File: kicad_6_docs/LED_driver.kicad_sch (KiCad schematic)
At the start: 18 parts, among them Q2 BC560, U14 SSI2164, U16 TL072

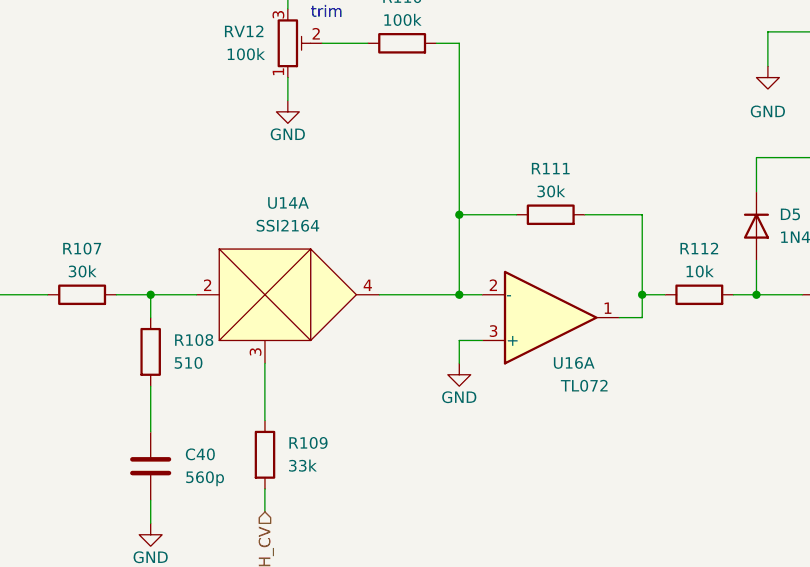
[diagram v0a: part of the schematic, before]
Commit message: Fix power supply errors, tidy up schematic
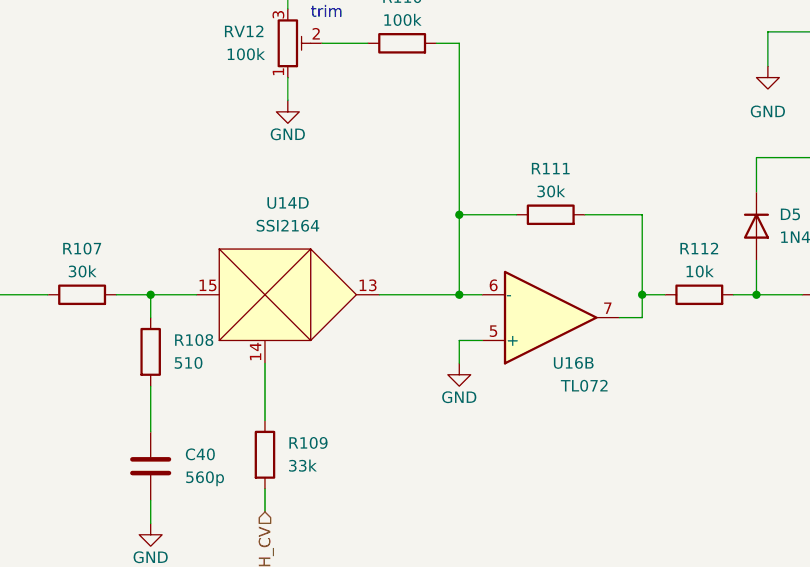
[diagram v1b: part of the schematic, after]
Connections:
- net GND: now also U16.5 (+); no longer U16.3 (+)
- net at R107.2, R108.1: now also U14.15; no longer U14.2
- net at R109.1: now also U14.14; no longer U14.3
- net at R110.2, R111.1: now also U14.13, U16.6 (-); no longer U14.4, U16.2 (-)
- net at R111.2, R112.1: now also U16.7; no longer U16.1
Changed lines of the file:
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@@
   (title_block
     (title "Mu-Tron Bi-Phase near-clone")
-    (date "2022-01-14")
+    (date "2022-08-01")
     (rev "0")
     (comment 2 "creativecommons.org/licenses/by/4.0/")
@@
     (effects (font (size 1.27 1.27)) (justify right))
   )
-  (symbol (lib_id "Device:LED") (at 194.31 111.76 90)
+  (symbol (lib_id "Device:LED") (at 194.31 111.76 90) (unit 1)
     (in_bom yes) (on_board yes) (fields_autoplaced)
     (property "Reference" "D7" (id 0) (at 198.12 112.0774 90)
@@
     (pin "2")
   )
-  (symbol (lib_id "Device:C") (at 114.3 109.22 0)
+  (symbol (lib_id "Device:C") (at 114.3 109.22 0) (unit 1)
     (in_bom yes) (on_board yes) (fields_autoplaced)
     (property "Reference" "C40" (id 0) (at 118.11 107.9499 0)
@@
     (pin "2")
   )
-  (symbol (lib_id "power:GND") (at 148.59 97.79 0)
+  (symbol (lib_id "power:GND") (at 148.59 97.79 0) (unit 1)
     (in_bom yes) (on_board yes)
     (property "Reference" "#PWR078" (id 0) (at 148.59 104.14 0)
@@
     (pin "1")
   )
-  (symbol (lib_id "power:GND") (at 114.3 115.57 0)
+  (symbol (lib_id "power:GND") (at 114.3 115.57 0) (unit 1)
     (in_bom yes) (on_board yes)
     (property "Reference" "#PWR075" (id 0) (at 114.3 121.92 0)
@@
     (pin "1")
   )
-  (symbol (lib_id "Device:R") (at 114.3 96.52 0)
+  (symbol (lib_id "Device:R") (at 114.3 96.52 0) (unit 1)
     (in_bom yes) (on_board yes) (fields_autoplaced)
     (property "Reference" "R108" (id 0) (at 116.84 95.2499 0)
@@
     (pin "2")
   )
-  (symbol (lib_id "custom_symbols:SSI2164") (at 127 90.17 0)
+  (symbol (lib_id "custom_symbols:SSI2164") (at 127 90.17 0) (unit 4)
     (in_bom yes) (on_board yes) (fields_autoplaced)
     (property "Reference" "U14" (id 0) (at 129.54 80.01 0))
@@
       (effects (font (size 1.27 1.27)) hide)
     )
+    (pin "2")
+    (pin "3")
+    (pin "4")
+    (pin "5")
+    (pin "6")
+    (pin "7")
+    (pin "10")
+    (pin "11")
+    (pin "12")
     (pin "13")
     (pin "14")
     (pin "15")
-  )
-  (symbol (lib_id "power:GND") (at 87.63 96.52 0)
+    (pin "1")
+    (pin "16")
+    (pin "8")
+    (pin "9")
+  )
+  (symbol (lib_id "power:GND") (at 87.63 96.52 0) (unit 1)
     (in_bom yes) (on_board yes)
     (property "Reference" "#PWR074" (id 0) (at 87.63 102.87 0)
@@
     (pin "1")
   )
-  (symbol (lib_id "power:GND") (at 129.54 68.58 0)
+  (symbol (lib_id "power:GND") (at 129.54 68.58 0) (unit 1)
     (in_bom yes) (on_board yes)
     (property "Reference" "#PWR077" (id 0) (at 129.54 74.93 0)
@@
     (pin "1")
   )
-  (symbol (lib_id "Diode:1N4148") (at 181.61 82.55 270)
+  (symbol (lib_id "Diode:1N4148") (at 181.61 82.55 270) (unit 1)
     (in_bom yes) (on_board yes) (fields_autoplaced)
     (property "Reference" "D5" (id 0) (at 184.15 81.2799 90)
@@
     (pin "2")
   )
-  (symbol (lib_id "biPhase_2-rescue:BC560") (at 191.77 90.17 0) (mirror x)
+  (symbol (lib_id "biPhase_2-rescue:BC560") (at 191.77 90.17 0) (mirror x) (unit 1)
     (in_bom yes) (on_board yes) (fields_autoplaced)
     (property "Reference" "Q2" (id 0) (at 196.85 88.265 0)
@@
     (pin "3")
   )
-  (symbol (lib_id "Device:LED") (at 194.31 101.6 90)
+  (symbol (lib_id "Device:LED") (at 194.31 101.6 90) (unit 1)
     (in_bom yes) (on_board yes) (fields_autoplaced)
     (property "Reference" "D6" (id 0) (at 198.12 101.9174 90)
@@
     (pin "2")
   )
-  (symbol (lib_id "Device:R") (at 106.68 90.17 90)
+  (symbol (lib_id "Device:R") (at 106.68 90.17 90) (unit 1)
     (in_bom yes) (on_board yes)
     (property "Reference" "R107" (id 0) (at 106.68 85.09 90))
@@
     (pin "2")
   )
-  (symbol (lib_id "power:+15V") (at 129.54 55.88 0)
+  (symbol (lib_id "power:+15V") (at 129.54 55.88 0) (unit 1)
     (in_bom yes) (on_board yes)
     (property "Reference" "#PWR076" (id 0) (at 129.54 59.69 0)
@@
     (pin "1")
   )
-  (symbol (lib_id "power:-15V") (at 194.31 128.27 180)
+  (symbol (lib_id "power:-15V") (at 194.31 128.27 180) (unit 1)
     (in_bom yes) (on_board yes)
     (property "Reference" "#PWR080" (id 0) (at 194.31 130.81 0)
@@
     (pin "1")
   )
-  (symbol (lib_id "Device:R") (at 194.31 68.58 0)
+  (symbol (lib_id "Device:R") (at 194.31 68.58 0) (unit 1)
     (in_bom yes) (on_board yes) (fields_autoplaced)
     (property "Reference" "R113" (id 0) (at 196.85 67.3099 0)
@@
     (pin "2")
   )
-  (symbol (lib_id "Device:R") (at 175.26 90.17 90)
+  (symbol (lib_id "Device:R") (at 175.26 90.17 90) (unit 1)
     (in_bom yes) (on_board yes)
     (property "Reference" "R112" (id 0) (at 175.26 85.09 90))
@@
     (pin "2")
   )
-  (symbol (lib_id "Device:R") (at 142.24 62.23 90)
+  (symbol (lib_id "Device:R") (at 142.24 62.23 90) (unit 1)
     (in_bom yes) (on_board yes)
     (property "Reference" "R110" (id 0) (at 142.24 57.15 90))
@@
     (pin "2")
   )
-  (symbol (lib_id "Device:R_Potentiometer_Trim") (at 87.63 90.17 0) (mirror x)
+  (symbol (lib_id "Device:R_Potentiometer_Trim") (at 87.63 90.17 0) (mirror x) (unit 1)
     (in_bom yes) (on_board yes) (fields_autoplaced)
     (property "Reference" "RV11" (id 0) (at 85.09 88.8999 0)
@@
     (pin "3")
   )
-  (symbol (lib_id "Device:R") (at 158.75 81.28 90)
+  (symbol (lib_id "Device:R") (at 158.75 81.28 90) (unit 1)
     (in_bom yes) (on_board yes)
     (property "Reference" "R111" (id 0) (at 158.75 76.2 90))
@@
     (pin "2")
   )
-  (symbol (lib_id "Device:R") (at 127 107.95 0)
+  (symbol (lib_id "Device:R") (at 127 107.95 0) (unit 1)
     (in_bom yes) (on_board yes) (fields_autoplaced)
     (property "Reference" "R109" (id 0) (at 129.54 106.6799 0)
@@
     (pin "2")
   )
-  (symbol (lib_id "Device:R_Potentiometer_Trim") (at 129.54 62.23 0) (mirror x)
+  (symbol (lib_id "Device:R_Potentiometer_Trim") (at 129.54 62.23 0) (mirror x) (unit 1)
     (in_bom yes) (on_board yes) (fields_autoplaced)
     (property "Reference" "RV12" (id 0) (at 127 60.9599 0)
@@
     (pin "3")
   )
-  (symbol (lib_id "power:GND") (at 182.88 64.77 0)
+  (symbol (lib_id "power:GND") (at 182.88 64.77 0) (unit 1)
     (in_bom yes) (on_board yes) (fields_autoplaced)
     (property "Reference" "#PWR079" (id 0) (at 182.88 71.12 0)
@@
     (pin "1")
   )
-  (symbol (lib_id "Device:R") (at 81.28 83.82 90)
+  (symbol (lib_id "Device:R") (at 81.28 83.82 90) (unit 1)
     (in_bom yes) (on_board yes)
     (property "Reference" "R106" (id 0) (at 81.28 78.74 90))
@@
     (pin "2")
   )
-  (symbol (lib_id "Amplifier_Operational:TL072") (at 158.75 92.71 0) (mirror x)
+  (symbol (lib_id "Amplifier_Operational:TL072") (at 158.75 92.71 0) (mirror x) (unit 2)
     (in_bom yes) (on_board yes)
     (property "Reference" "U16" (id 0) (at 161.29 97.79 0))
@@
       (effects (font (size 1.27 1.27)) hide)
     )
+    (pin "1")
+    (pin "2")
+    (pin "3")
     (pin "5")
     (pin "6")
     (pin "7")
-  )
-  (symbol (lib_id "Device:LED") (at 194.31 121.92 90)
+    (pin "4")
+    (pin "8")
+  )
+  (symbol (lib_id "Device:LED") (at 194.31 121.92 90) (unit 1)
     (in_bom yes) (on_board yes) (fields_autoplaced)
     (property "Reference" "D8" (id 0) (at 198.12 122.2374 90)
